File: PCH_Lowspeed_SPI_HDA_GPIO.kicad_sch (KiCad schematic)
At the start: 5 parts

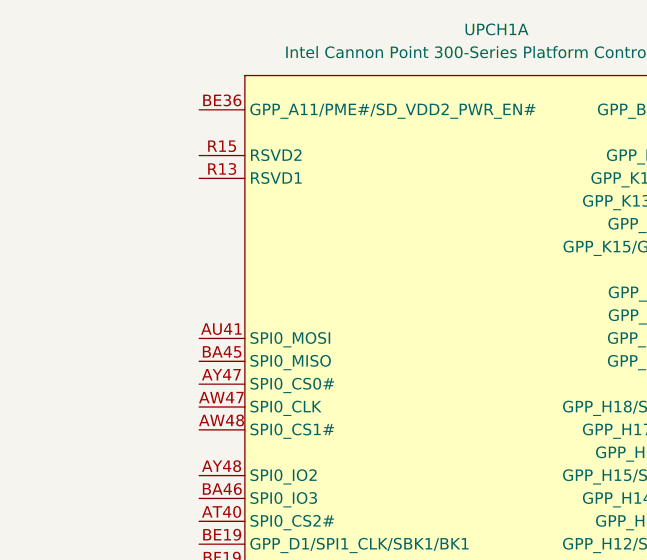
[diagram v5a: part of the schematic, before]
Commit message: Fixed 2 pins that somehow disappeared from schematic
i blame my kicad libraries being weird lol
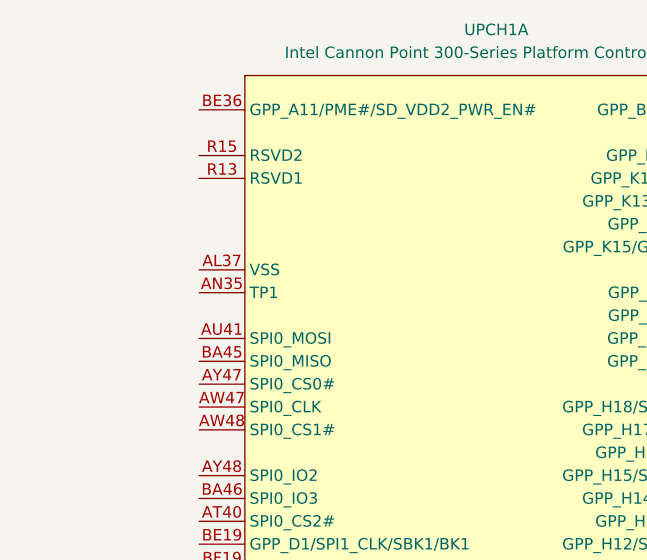
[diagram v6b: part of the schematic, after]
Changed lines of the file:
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@@
 		(pin "G2"
 		)
+		(pin "AN35"
+		)
+		(pin "AL37"
+		)
 		(instances
 			(project ""
@@
 		(pin "G2"
 		)
+		(pin "AL37"
+		)
+		(pin "AN35"
+		)
 		(instances
 			(project ""
@@
 		(pin "G2"
 		)
+		(pin "AL37"
+		)
+		(pin "AN35"
+		)
 		(instances
 			(project ""
@@
 		(pin "G2"
 		)
+		(pin "AL37"
+		)
+		(pin "AN35"
+		)
 		(instances
 			(project ""
@@
 		(pin "G2"
 		)
+		(pin "AN35"
+		)
+		(pin "AL37"
+		)
 		(instances
